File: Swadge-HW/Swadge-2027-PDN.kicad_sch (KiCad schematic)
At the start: 11 parts, among them SW9 SW_SPDT_1825232-1, U3 XB7608AJ

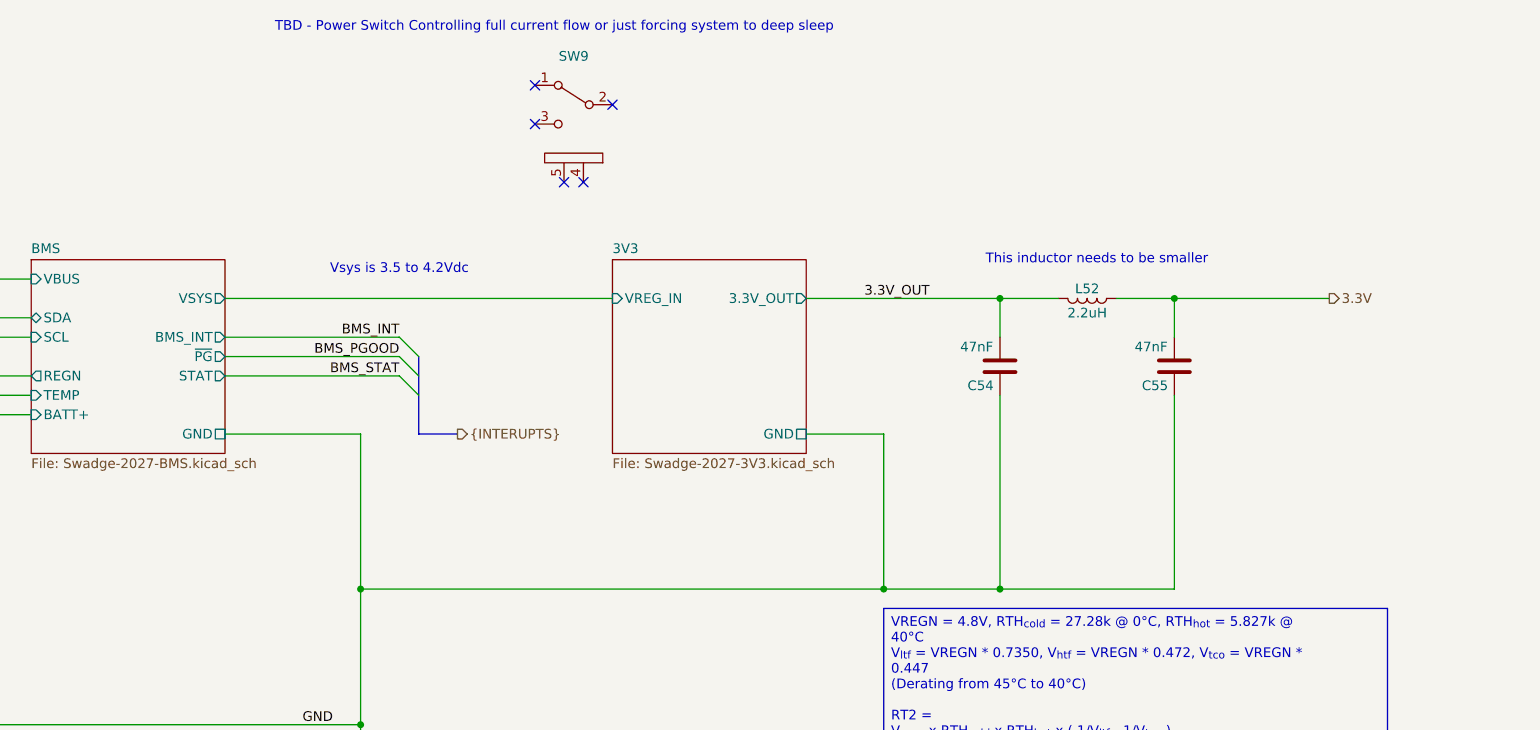
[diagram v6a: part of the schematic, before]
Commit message: Routing Updates
Added Power Switch
Routed More
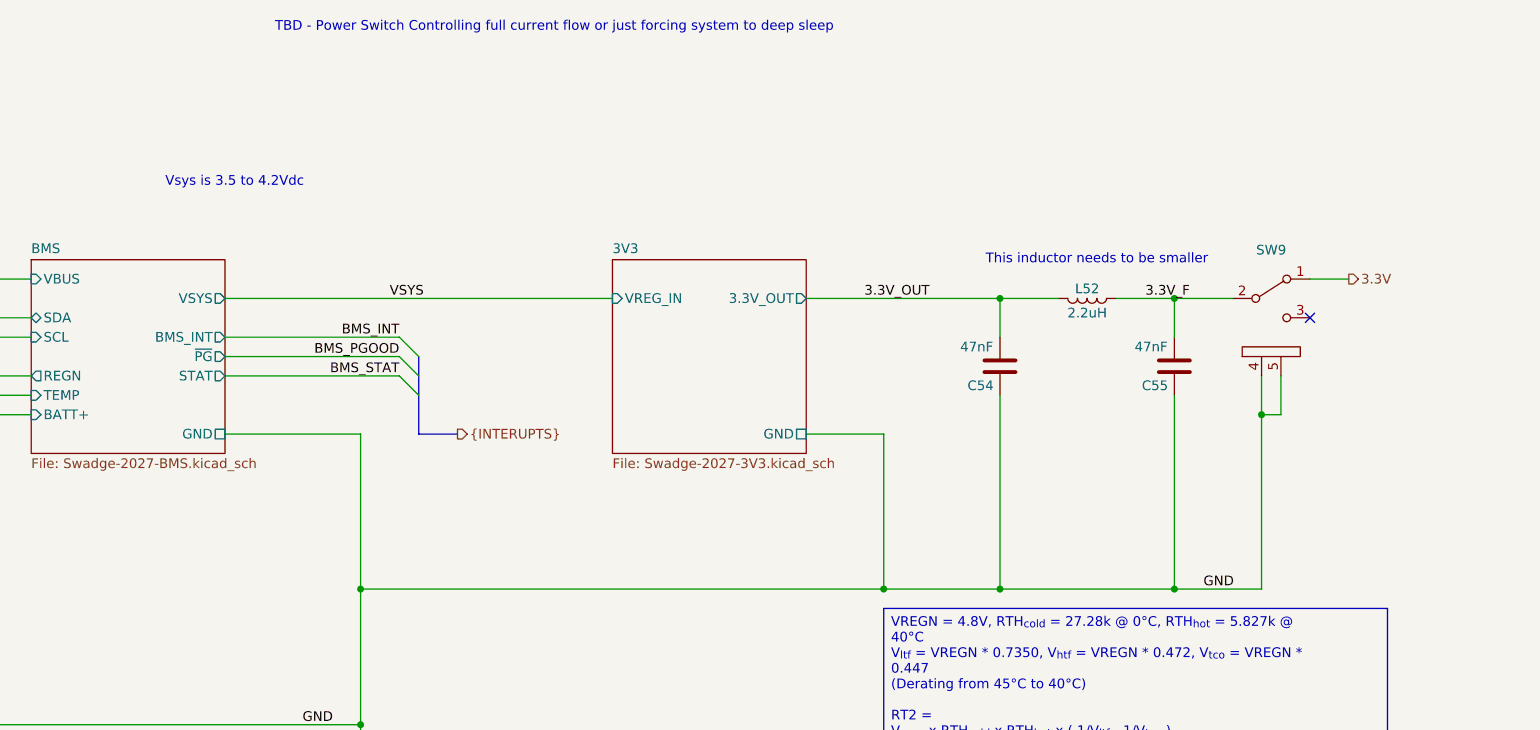
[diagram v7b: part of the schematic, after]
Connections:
- net 3.3V: now also SW9.1 (A); no longer C55.1, L52.1
- net GND: now also SW9.4 (D), SW9.5 (E)
- net 3.3V_F: now reaches SW9.2 (B)
- net 3.3V_F: now also C55.1, L52.1
- no-connect marks 5 -> 1
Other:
- moved on the sheet: SW9
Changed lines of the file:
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@@
 	(text "Vsys is 3.5 to 4.2Vdc"
 		(exclude_from_sim no)
-		(at 149.86 52.07 0)
+		(at 128.27 40.64 0)
 		(effects
 			(font
@@
 	)
 	(junction
+		(at 251.46 55.88)
+		(diameter 0)
+		(color 0 0 0 0)
+	)
+	(junction
+		(at 262.89 71.12)
+		(diameter 0)
+		(color 0 0 0 0)
+	)
+	(junction
 		(at 27.94 137.16)
 		(diameter 0)
@@
 	)
 	(junction
+		(at 251.46 93.98)
+		(diameter 0)
+		(color 0 0 0 0)
+	)
+	(junction
 		(at 88.9 111.76)
 		(diameter 0)
@@
 	)
 	(junction
-		(at 251.46 55.88)
-		(diameter 0)
-		(color 0 0 0 0)
-	)
-	(junction
 		(at 228.6 55.88)
 		(diameter 0)
@@
 	)
 	(no_connect
-		(at 173.99 40.64)
-	)
-	(no_connect
-		(at 167.64 27.94)
-	)
-	(no_connect
-		(at 171.45 40.64)
-	)
-	(no_connect
-		(at 177.8 30.48)
-	)
-	(no_connect
-		(at 167.64 33.02)
+		(at 269.24 58.42)
 	)
 	(bus_entry
@@
 	(wire
 		(pts
+			(xy 127 55.88) (xy 177.8 55.88)
+		)
+		(stroke
+			(width 0)
+			(type default)
+		)
+	)
+	(wire
+		(pts
 			(xy 213.36 73.66) (xy 213.36 93.98)
 		)
@@
 	(wire
 		(pts
+			(xy 251.46 55.88) (xy 259.08 55.88)
+		)
+		(stroke
+			(width 0)
+			(type default)
+		)
+	)
+	(wire
+		(pts
 			(xy 127 66.04) (xy 149.86 66.04)
 		)
@@
 	(wire
 		(pts
+			(xy 262.89 93.98) (xy 262.89 71.12)
+		)
+		(stroke
+			(width 0)
+			(type default)
+		)
+	)
+	(wire
+		(pts
 			(xy 68.58 58.42) (xy 101.6 58.42)
 		)
@@
 	(wire
 		(pts
+			(xy 262.89 66.04) (xy 262.89 71.12)
+		)
+		(stroke
+			(width 0)
+			(type default)
+		)
+	)
+	(wire
+		(pts
 			(xy 127 63.5) (xy 149.86 63.5)
 		)
@@
 	(wire
 		(pts
-			(xy 251.46 55.88) (xy 271.78 55.88)
-		)
-		(stroke
-			(width 0)
-			(type default)
-		)
-	)
-	(wire
-		(pts
 			(xy 15.24 137.16) (xy 15.24 139.7)
 		)
@@
 	(wire
 		(pts
-			(xy 127 55.88) (xy 177.8 55.88)
-		)
-		(stroke
-			(width 0)
-			(type default)
-		)
-	)
-	(wire
-		(pts
 			(xy 78.74 139.7) (xy 68.58 139.7)
 		)
@@
 	(wire
 		(pts
+			(xy 262.89 71.12) (xy 265.43 71.12)
+		)
+		(stroke
+			(width 0)
+			(type default)
+		)
+	)
+	(wire
+		(pts
 			(xy 27.94 137.16) (xy 15.24 137.16)
 		)
@@
 	(wire
 		(pts
+			(xy 251.46 93.98) (xy 262.89 93.98)
+		)
+		(stroke
+			(width 0)
+			(type default)
+		)
+	)
+	(wire
+		(pts
+			(xy 269.24 53.34) (xy 274.32 53.34)
+		)
+		(stroke
+			(width 0)
+			(type default)
+		)
+	)
+	(wire
+		(pts
 			(xy 144.78 93.98) (xy 213.36 93.98)
+		)
+		(stroke
+			(width 0)
+			(type default)
+		)
+	)
+	(wire
+		(pts
+			(xy 265.43 66.04) (xy 265.43 71.12)
 		)
 		(stroke
@@
 		)
 	)
+	(label "VSYS"
+		(at 148.59 55.88 0)
+		(effects
+			(font
+				(size 1.27 1.27)
+			)
+			(justify left bottom)
+		)
+	)
 	(label "TEMP"
 		(at 91.44 68.58 0)
@@
 		)
 	)
+	(label "GND"
+		(at 255.27 93.98 0)
+		(effects
+			(font
+				(size 1.27 1.27)
+			)
+			(justify left bottom)
+		)
+	)
 	(label "I2C_SDA"
 		(at 68.58 58.42 0)
@@
 		)
 	)
+	(label "3.3V_F"
+		(at 247.65 55.88 0)
+		(effects
+			(font
+				(size 1.27 1.27)
+			)
+			(justify left bottom)
+		)
+	)
 	(label "TEMP"
 		(at 38.1 137.16 180)
@@
 	(hierarchical_label "3.3V"
 		(shape output)
-		(at 271.78 55.88 0)
+		(at 274.32 53.34 0)
 		(effects
 			(font
@@
 	(symbol
 		(lib_id "Swadge_Parts:SW_SPDT_1825232-1")
-		(at 172.72 30.48 0)
-		(mirror y)
+		(at 264.16 55.88 0)
 		(unit 1)
 		(body_style 1)
@@
 		(dnp no)
 		(property "Reference" "SW9"
-			(at 172.72 24.13 0)
+			(at 264.16 49.53 0)
 			(show_name no)
 			(do_not_autoplace no)
@@
 		)
 		(property "Value" "SW_SPDT_1825232-1"
-			(at 156.972 30.988 0)
+			(at 279.908 56.388 0)
 			(hide yes)
 			(show_name no)
@@
 		)
 		(property "Footprint" "Swadge_Parts:1825232-1"
-			(at 172.72 13.97 0)
+			(at 264.16 39.37 0)
 			(hide yes)
 			(show_name no)
@@
 		)
 		(property "Datasheet" "https://datasheet.lcsc.com/lcsc/1912111437_SHOU-HAN-SK12D07VG4_C393937.pdf"
-			(at 172.72 16.51 0)
+			(at 264.16 41.91 0)
 			(hide yes)
 			(show_name no)
@@
 		)
 		(property "Description" "Slide Switch SPDT Through Hole, Right Angle"
-			(at 172.72 30.48 0)
+			(at 264.16 55.88 0)
 			(hide yes)
 			(show_name no)
@@
 		)
 		(property "Digikey" "A107673-ND"
-			(at 172.72 19.05 0)
+			(at 264.16 44.45 0)
 			(hide yes)
 			(show_name no)
@@
 		)
 		(property "Cost100" "45"
-			(at 172.72 11.43 0)
+			(at 264.16 36.83 0)
 			(hide yes)
 			(show_name no)
@@
 		)
 		(property "Substitutable" "Y"
-			(at 172.72 30.48 0)
+			(at 264.16 55.88 0)
 			(hide yes)
 			(show_name no)
@@
 		)
 		(property "Notes" "Use SPDT slide switch. Similar to 1825232-1"
-			(at 172.72 21.59 0)
+			(at 264.16 46.99 0)
 			(hide yes)
 			(show_name no)
@@
 		)
 		(property "LCSC" "C393937"
-			(at 172.72 30.48 0)
+			(at 264.16 55.88 0)
 			(hide yes)
 			(show_name no)
@@
 		)
 		(property "Cost @ 2.5k" "0.0123"
-			(at 172.72 30.48 0)
-			(hide yes)
-			(show_name no)
+			(at 264.16 55.88 0)
+			(hide yes)
+			(show_name no)

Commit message: Update Library Links
Point to Swadge Parts link
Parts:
- BT1: symbol Swadge_Parts:1x18650_Battery_Holder -> Swadge_Parts:BH-18650-B
- U3: symbol sao:XB7608AJ -> Swadge_Parts:XB7608AJ
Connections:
- net BATT+: now also BT1.2 (+); no longer BT1.1 (+)
- net BATT-: now also BT1.1 (-); no longer BT1.2 (-)
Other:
- moved on the sheet: BT1
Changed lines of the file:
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@@
 	)
 	(symbol
-		(lib_id "sao:XB7608AJ")
+		(lib_id "Swadge_Parts:XB7608AJ")
 		(at 93.98 144.78 0)
 		(unit 1)
@@
 		)
 		(property "Footprint" "Swadge_Parts:CPC-5_2.6mmx4mm_P0.53mm"
-			(at 93.98 144.78 0)
+			(at 93.98 167.64 0)
 			(hide yes)
 			(show_name no)
@@
 			)
 		)
-		(property "Description" ""
-			(at 93.98 144.78 0)
+		(property "Description" "Battery Safety Isolator"
+			(at 93.98 165.1 0)
 			(hide yes)
 			(show_name no)
@@
 	)
 	(symbol
-		(lib_id "Swadge_Parts:1x18650_Battery_Holder")
-		(at 50.8 144.78 0)
+		(lib_id "Swadge_Parts:BH-18650-B")
+		(at 50.8 144.78 270)
 		(unit 1)
 		(body_style 1)
@@
 		(fields_autoplaced yes)
 		(property "Reference" "BT1"
-			(at 53.467 143.5678 0)
+			(at 53.467 143.5678 90)
 			(show_name no)
 			(do_not_autoplace no)
@@
 		)
 		(property "Value" "Battery Holder"
-			(at 53.467 145.9921 0)
+			(at 53.467 145.9921 90)
 			(show_name no)
 			(do_not_autoplace no)
@@
 		)
 		(property "Footprint" "Swadge_Parts:BH-18650-Bxxx002"
-			(at 53.467 140.7625 0)
+			(at 54.8175 147.447 0)
 			(hide yes)
 			(show_name no)
@@
 		)
 		(property "Datasheet" "https://www.lcsc.com/datasheet/C2988620.pdf"
-			(at 53.467 143.1868 0)
+			(at 52.3932 147.447 0)
 			(hide yes)
 			(show_name no)
@@
 		)
 		(property "Description" "BATT HOLDER, 18650, 1 CELL SMD"
-			(at 53.467 145.6111 0)
+			(at 49.9689 147.447 0)
 			(hide yes)
 			(show_name no)
@@
 		)
 		(property "Digikey" "36-1042P-ND"
-			(at 53.467 148.0354 0)
+			(at 47.5446 147.447 0)
 			(hide yes)
 			(show_name no)
@@
 		)
 		(property "Substitutable" "Y"
-			(at 53.467 150.4597 0)
+			(at 45.1203 147.447 0)
 			(hide yes)
 			(show_name no)
@@
 		)
 		(property "Notes" ""
-			(at 53.467 152.884 0)
+			(at 42.696 147.447 0)
 			(hide yes)
 			(show_name no)
@@
 		)
 		(property "LCSC" "C2988620"
-			(at 58.42 152.4 0)
+			(at 43.18 152.4 0)
 			(hide yes)
 			(show_name no)
@@
 		)
 		(property "Cost @ 2.5k" "0.9186"
-			(at 55.88 154.94 0)
-			(hide yes)
-			(show_name no)
+			(at 40.64 149.86 0)
+			(hide yes)
+			(show_name no)
